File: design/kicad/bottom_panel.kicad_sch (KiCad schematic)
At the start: 31 parts, among them J1 AudioJack3, J3 AudioJack3, U1 TL072, U2 6N138M, U3 PCA9685PW

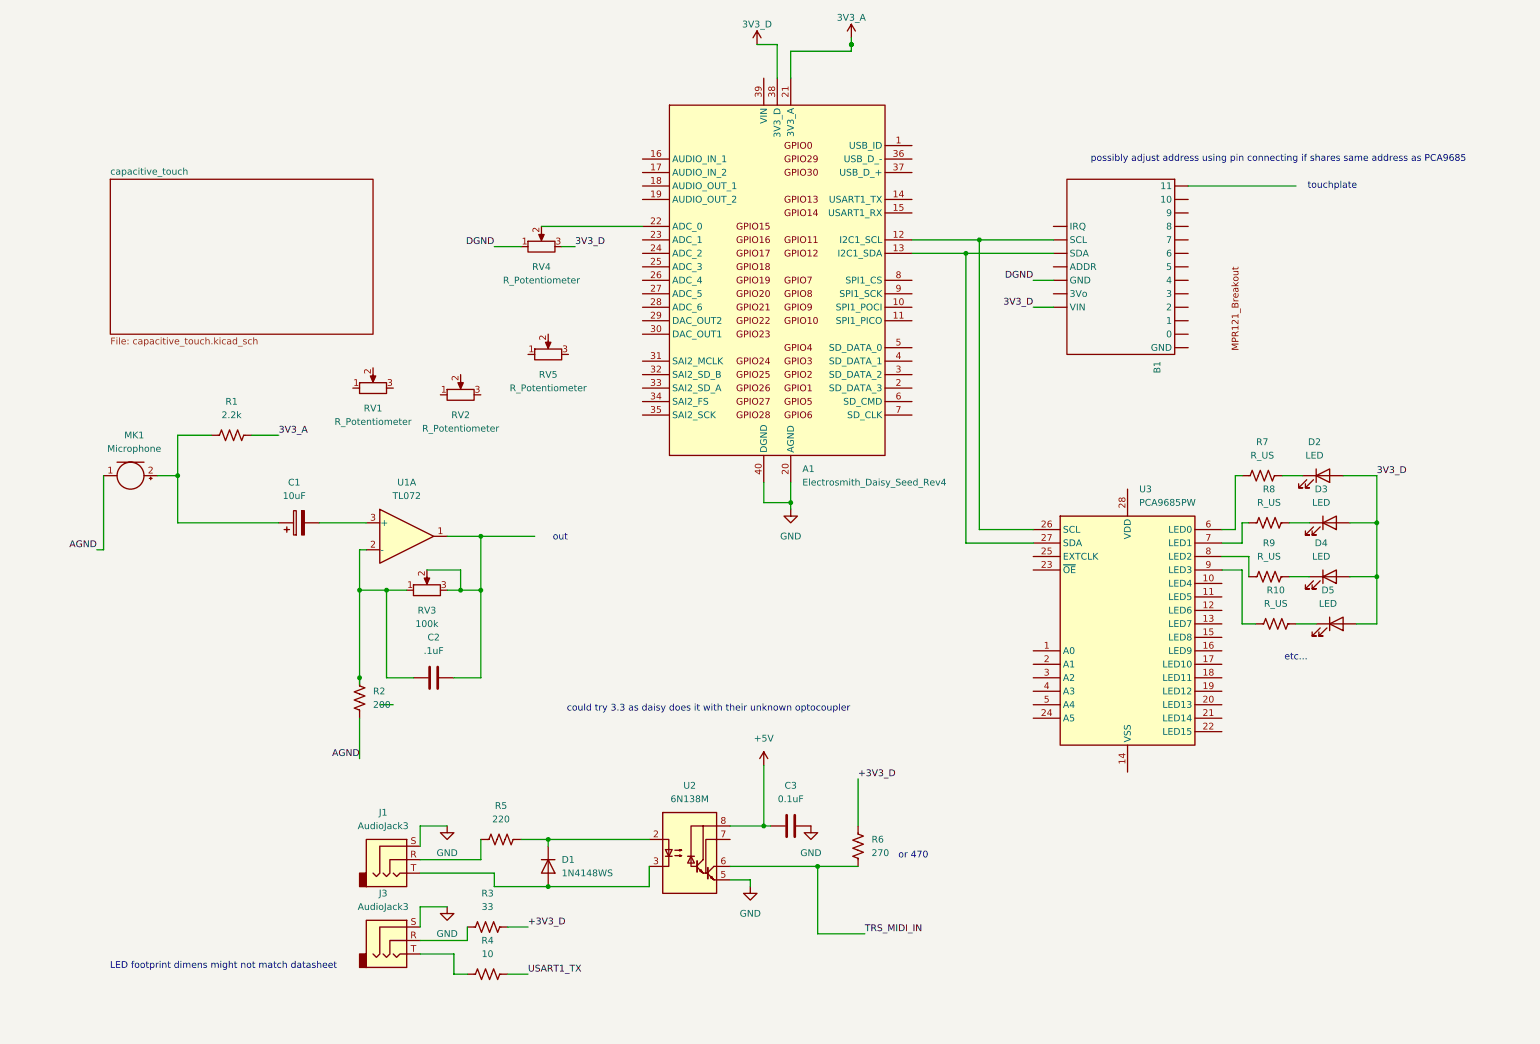
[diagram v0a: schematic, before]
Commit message: Refactors design for flat schematic, adds capactive touch, LCSC parts
did not use bss138 level shifters and regulated 3.3v supply from adafruit schematic because daisy seed already has 3.3v regulated supply and 5V is not used internally on seed
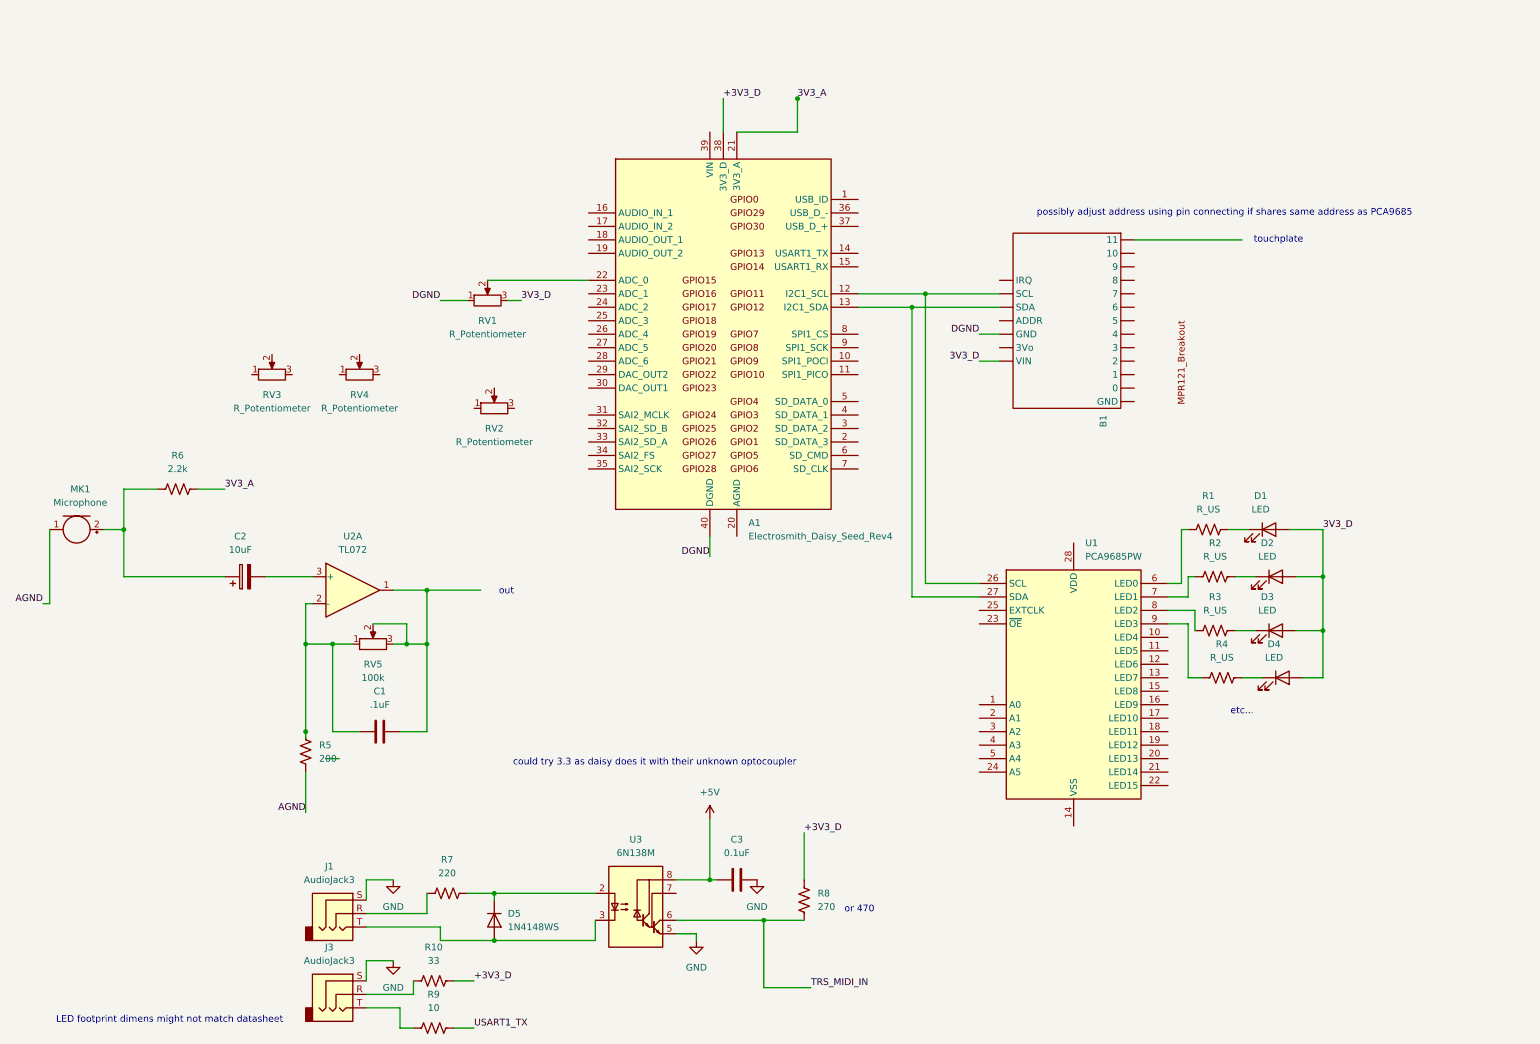
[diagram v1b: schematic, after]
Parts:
- removed C1: 10uF, symbol Device:C_Polarized
- removed C2: .1uF, symbol Device:C
- removed D1: 1N4148WS, Diode_SMD:D_SOD-323, symbol Diode:1N4148WS
- removed D5: LED, LED_SMD:LED_PLCC-2_3.4x3.0mm_AK, symbol Device:LED
- removed U1: TL072, symbol Amplifier_Operational:TL072
- removed U2: 6N138M, symbol Isolator:6N138
- removed U3: PCA9685PW, Package_SO:TSSOP-28_4.4x9.7mm_P0.65mm, symbol Driver_LED:PCA9685PW
- added C1: .1uF, symbol Device:C
- added C2: 10uF, symbol Device:C_Polarized
- added D1: LED, LED_SMD:LED_PLCC-2_3.4x3.0mm_AK, symbol Device:LED
- added D5: 1N4148WS, Diode_SMD:D_SOD-323, symbol Diode:1N4148WS
- added U1: PCA9685PW, Package_SO:TSSOP-28_4.4x9.7mm_P0.65mm, symbol Driver_LED:PCA9685PW
- added U2: TL072, symbol Amplifier_Operational:TL072
- added U3: 6N138M, symbol Isolator:6N138
- R1: value 2.2k -> R_US
- R10: value R_US -> 33
- R2: value 200 -> R_US
- R3: value 33 -> R_US
- R4: value 10 -> R_US
- R5: value 220 -> 200
- R6: value 270 -> 2.2k
- R7: value R_US -> 220
- R8: value R_US -> 270
- R9: value R_US -> 10
- RV3: value 100k -> R_Potentiometer
- RV5: value R_Potentiometer -> 100k
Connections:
- net +3V3_D: now also A1.38 (3V3_D), R10.2, R8.2; no longer R3.2, R6.2
- net +5V: now also U3.8 (VCC)
- net 3V3_A: now also R6.2; no longer R1.2
- net 3V3_D: now also RV1.3, D1.2 (A); no longer A1.38 (3V3_D), RV4.3
- net AGND: now also R5.1; no longer R2.1
- net DGND: now also A1.40 (DGND), RV1.1; no longer RV4.1
- net GND: now also U3.5 (GND); no longer A1.20 (AGND), A1.40 (DGND)
- net TRS_MIDI_IN: now also R8.1, U3.6 (VO2); no longer R6.1
- net USART1_TX: now also R9.2; no longer R4.2
- net at MK1.2 (+): now also R6.1, C2.1; no longer R1.1
- net at A1.12 (I2C1_SCL), B1. (VIN): now also U1.26 (SCL)
- net at A1.13 (I2C1_SDA), B1. (VIN): now also U1.27 (SDA)
- net at R10.1: now also J3.R
- net at RV3.1: no longer R2.2
- net at RV5.1: now also R5.2, C1.1, U2.2 (-)
- net at RV5.2: now also RV5.3, C1.2, U2.1
- net at J1.R: now also R7.1; no longer R5.1
- net at J1.T: now also D5.2 (A), U3.3 (C2)
- net at D3.1 (K): now also R3.2; no longer R8.2
- net at RV1.2: now also A1.22 (ADC_0)
- net at R3.1: now also U1.8 (LED2); no longer J3.R
- net at R4.1: now also U1.9 (LED3); no longer J3.T
- net at RV3.2: no longer RV3.3
- net at R9.1: now also J3.T
- net at D4.1 (K): now also R4.2; no longer R9.2
- net at D2.1 (K): now also R2.2; no longer R7.2
- net at RV4.2: no longer A1.22 (ADC_0)
- new net: C2.2, U2.3 (+)
- new net: R2.1, U1.7 (LED1)
- new net: R1.1, U1.6 (LED0)
- new net: D1.1 (K), R1.2
- new net: D5.1 (K), R7.2, U3.2 (C1)
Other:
- removed sheet capacitive_touch
